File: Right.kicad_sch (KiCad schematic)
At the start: 0 parts

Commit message: finish left side. do a bunch of right side. do right db. change db flat ribbon on both
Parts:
- added C101, C105: 4.7uF, Capacitor_SMD:C_0402_1005Metric, symbol Device:C_Small
- added C102, C103, C107, C108, C109, C110, C111, C112, C113, C114, C115, C116, C118, C120: 1uF, Capacitor_SMD:C_0402_1005Metric, symbol Device:C_Small
- added C104, C106: .1uF, Capacitor_SMD:C_0402_1005Metric, symbol Device:C_Small
- added C117, C119: 2.2uF, Capacitor_SMD:C_0402_1005Metric, symbol Device:C_Small
- added CH_SW101: GESC, marbastlib-choc:SW_choc_HS_1u, symbol MX_Alps_Hybrid:MX-NoLED
- added CH_SW102: 1, marbastlib-choc:SW_choc_HS_1u, symbol MX_Alps_Hybrid:MX-NoLED
- added CH_SW103: 2, marbastlib-choc:SW_choc_HS_1u, symbol MX_Alps_Hybrid:MX-NoLED
- added CH_SW104: 3, marbastlib-choc:SW_choc_HS_1u, symbol MX_Alps_Hybrid:MX-NoLED
- added CH_SW105: 4, marbastlib-choc:SW_choc_HS_1u, symbol MX_Alps_Hybrid:MX-NoLED
- added CH_SW106: 5, marbastlib-choc:SW_choc_HS_1u, symbol MX_Alps_Hybrid:MX-NoLED
- added CH_SW107: TAB, marbastlib-choc:SW_choc_HS_1u, symbol MX_Alps_Hybrid:MX-NoLED
- added CH_SW108: Q, marbastlib-choc:SW_choc_HS_1u, symbol MX_Alps_Hybrid:MX-NoLED
- added CH_SW109: w, marbastlib-choc:SW_choc_HS_1u, symbol MX_Alps_Hybrid:MX-NoLED
- added CH_SW110: E, marbastlib-choc:SW_choc_HS_1u, symbol MX_Alps_Hybrid:MX-NoLED
- added CH_SW111: R, marbastlib-choc:SW_choc_HS_1u, symbol MX_Alps_Hybrid:MX-NoLED
- added CH_SW112: T, marbastlib-choc:SW_choc_HS_1u, symbol MX_Alps_Hybrid:MX-NoLED
- added CH_SW113: CAPS, marbastlib-choc:SW_choc_HS_1u, symbol MX_Alps_Hybrid:MX-NoLED
- added CH_SW114: A, marbastlib-choc:SW_choc_HS_1u, symbol MX_Alps_Hybrid:MX-NoLED
- added CH_SW115: S, marbastlib-choc:SW_choc_HS_1u, symbol MX_Alps_Hybrid:MX-NoLED
- added CH_SW116: D, marbastlib-choc:SW_choc_HS_1u, symbol MX_Alps_Hybrid:MX-NoLED
- added CH_SW117: F, marbastlib-choc:SW_choc_HS_1u, symbol MX_Alps_Hybrid:MX-NoLED
- added CH_SW118: G, marbastlib-choc:SW_choc_HS_1u, symbol MX_Alps_Hybrid:MX-NoLED
- added CH_SW119: SHIFT, marbastlib-choc:SW_choc_HS_1u, symbol MX_Alps_Hybrid:MX-NoLED
- added CH_SW120: Z, marbastlib-choc:SW_choc_HS_1u, symbol MX_Alps_Hybrid:MX-NoLED
- added CH_SW121: X, marbastlib-choc:SW_choc_HS_1u, symbol MX_Alps_Hybrid:MX-NoLED
- added CH_SW122: C, marbastlib-choc:SW_choc_HS_1u, symbol MX_Alps_Hybrid:MX-NoLED
- added CH_SW123: V, marbastlib-choc:SW_choc_HS_1u, symbol MX_Alps_Hybrid:MX-NoLED
- added CH_SW124: B, marbastlib-choc:SW_choc_HS_1u, symbol MX_Alps_Hybrid:MX-NoLED
- added CH_SW125: THUMB 2, marbastlib-choc:SW_choc_HS_1.5u, symbol MX_Alps_Hybrid:MX-NoLED
- added CH_SW126: CTRL, marbastlib-choc:SW_choc_HS_1u, symbol MX_Alps_Hybrid:MX-NoLED
- added CH_SW127: WIN, marbastlib-choc:SW_choc_HS_1u, symbol MX_Alps_Hybrid:MX-NoLED
- added CH_SW128: ALT, marbastlib-choc:SW_choc_HS_1u, symbol MX_Alps_Hybrid:MX-NoLED
- added CH_SW129: FN, marbastlib-choc:SW_choc_HS_1u, symbol MX_Alps_Hybrid:MX-NoLED
- added CH_SW130: THUMB 1, marbastlib-choc:SW_choc_HS_1.25u, symbol MX_Alps_Hybrid:MX-NoLED
- added D101: BAV70_Small, Package_TO_SOT_SMD:SOT-23, symbol marbastlib-various:BAV70_Small
- added D102, D103, D104, D105, D106, D107, D108, D109, D110, D111, D112, D113, D114, D115, D116: ~, Package_TO_SOT_SMD:SOT-23, symbol marbastlib-various:BAV70_Small
- added D117: D, Diode_SMD:D_SOD-123, symbol Device:D_Schottky_Small
- added F101: Polyfuse, Resistor_SMD:R_0805_2012Metric, symbol Device:Polyfuse
- added H101: M.2 Mount (M3), MountingHole:MountingHole_3.2mm_M3_DIN965_Pad, symbol Mechanical:MountingHole_Pad
- added J101: HRO-TYPEC-M12, marbastlib-various:USB_C_Receptacle_HRO_TYPE-C-31-M-14, symbol Connector:USB_C_Receptacle_USB2.0
- added J102, J106: DB FFC, Connector-pat-various:100519220810EHLF, symbol Connector_Generic:Conn_01x08
- added J103: DEBUG, Connector_PinSocket_2.54mm:PinSocket_2x03_P2.54mm_Vertical, symbol Connector_Generic:Conn_02x03_Odd_Even
- added J104: BATTERY, Connector_JST:JST_PH_S2B-PH-SM4-TB_1x02-1MP_P2.00mm_Horizontal, symbol Connector_Generic:Conn_01x02
- added J105: OLED, SSD1306:128x64OLED, symbol Connector_Generic:Conn_01x04
- added J107: SPLIT, Connector-pat-various:Magnetic Pogo 4 pin, symbol Connector_Generic:Conn_01x04
- added J108: EPAPER RIBBON, Connector-pat-various:100519223010ELF, symbol Connector_Generic:Conn_01x30
- added LO101: TapTap Logo, LogoSmall:tt_4mm, symbol Mechanical:MountingHole
- added LO102: MUD LOGO, LogoSmall:LogoSmall_Cu, symbol Switch:SW_SPST
- added M101: M.2_Key_E, m2ngff:m2-bracket-key-e, symbol m2ngff:M.2_Key_E
- added M102, M103: MOUNTING, MountingHole:MountingHole_2.2mm_M2_Pad, symbol Mechanical:MountingHole_Pad
- added MO101, MO102, MO103, MO104, MO105, MO106, MO107: Mousebite, marbastlib-various:mousebites_2mm, symbol Mechanical:MountingHole
- added MX_SW101: GESC, marbastlib-mx:SW_MX_HS_1u, symbol MX_Alps_Hybrid:MX-NoLED
- added MX_SW102: 1, marbastlib-mx:SW_MX_HS_1u, symbol MX_Alps_Hybrid:MX-NoLED
- added MX_SW103: 2, marbastlib-mx:SW_MX_HS_1u, symbol MX_Alps_Hybrid:MX-NoLED
- added MX_SW104: 3, marbastlib-mx:SW_MX_HS_1u, symbol MX_Alps_Hybrid:MX-NoLED
- added MX_SW105: 4, marbastlib-mx:SW_MX_HS_1u, symbol MX_Alps_Hybrid:MX-NoLED
- added MX_SW106: 5, marbastlib-mx:SW_MX_HS_1u, symbol MX_Alps_Hybrid:MX-NoLED
- added MX_SW107: TAB, marbastlib-mx:SW_MX_HS_1u, symbol MX_Alps_Hybrid:MX-NoLED
- added MX_SW108: Q, marbastlib-mx:SW_MX_HS_1u, symbol MX_Alps_Hybrid:MX-NoLED
- added MX_SW109: w, marbastlib-mx:SW_MX_HS_1u, symbol MX_Alps_Hybrid:MX-NoLED
- added MX_SW110: E, marbastlib-mx:SW_MX_HS_1u, symbol MX_Alps_Hybrid:MX-NoLED
- added MX_SW111: R, marbastlib-mx:SW_MX_HS_1u, symbol MX_Alps_Hybrid:MX-NoLED
- added MX_SW112: T, marbastlib-mx:SW_MX_HS_1u, symbol MX_Alps_Hybrid:MX-NoLED
- added MX_SW113: CAPS, marbastlib-mx:SW_MX_HS_1u, symbol MX_Alps_Hybrid:MX-NoLED
- added MX_SW114: A, marbastlib-mx:SW_MX_HS_1u, symbol MX_Alps_Hybrid:MX-NoLED
- added MX_SW115: S, marbastlib-mx:SW_MX_HS_1u, symbol MX_Alps_Hybrid:MX-NoLED
- added MX_SW116: D, marbastlib-mx:SW_MX_HS_1u, symbol MX_Alps_Hybrid:MX-NoLED
- added MX_SW117: F, marbastlib-mx:SW_MX_HS_1u, symbol MX_Alps_Hybrid:MX-NoLED
- added MX_SW118: G, marbastlib-mx:SW_MX_HS_1u, symbol MX_Alps_Hybrid:MX-NoLED
- added MX_SW119: SHIFT, marbastlib-mx:SW_MX_HS_1u, symbol MX_Alps_Hybrid:MX-NoLED
- added MX_SW120: Z, marbastlib-mx:SW_MX_HS_1u, symbol MX_Alps_Hybrid:MX-NoLED
- added MX_SW121: X, marbastlib-mx:SW_MX_HS_1u, symbol MX_Alps_Hybrid:MX-NoLED
- added MX_SW122: C, marbastlib-mx:SW_MX_HS_1u, symbol MX_Alps_Hybrid:MX-NoLED
- added MX_SW123: V, marbastlib-mx:SW_MX_HS_1u, symbol MX_Alps_Hybrid:MX-NoLED
- added MX_SW124: B, marbastlib-mx:SW_MX_HS_1u, symbol MX_Alps_Hybrid:MX-NoLED
- added MX_SW125: THUMB 2, marbastlib-mx:SW_MX_HS_1.5u, symbol MX_Alps_Hybrid:MX-NoLED
- added MX_SW126: CTRL, marbastlib-mx:SW_MX_HS_1u, symbol MX_Alps_Hybrid:MX-NoLED
- added MX_SW127: WIN, marbastlib-mx:SW_MX_HS_1u, symbol MX_Alps_Hybrid:MX-NoLED
- added MX_SW128: ALT, marbastlib-mx:SW_MX_HS_1u, symbol MX_Alps_Hybrid:MX-NoLED
- added MX_SW129: FN, marbastlib-mx:SW_MX_HS_1u, symbol MX_Alps_Hybrid:MX-NoLED
- added MX_SW130: THUMB 1, marbastlib-mx:SW_MX_HS_1.25u, symbol MX_Alps_Hybrid:MX-NoLED
- added MX_SW131: ISO, marbastlib-mx:SW_MX_HS_1u, symbol MX_Alps_Hybrid:MX-NoLED
- added R101, R102: 5.1k, Resistor_SMD:R_0402_1005Metric, symbol Device:R
- added R103, R104: 10K, Resistor_SMD:R_0402_1005Metric, symbol Device:R
- added R105, R106, R107: JUMPER, Resistor_SMD:R_0805_2012Metric, symbol Device:R_Small
- added S101: ISO STAB, Connector-pat-various:STAB_MX_ISONT, symbol marbastlib-mx:MX_stab
- added SW101: Battery Toggle, marbastlib-various:SW_MSK12C02-HB, symbol Switch:SW_SPST
- added U101: SRV05-4, marbastlib-various:SOT-23-6-routable, symbol Power_Protection:SRV05-4
- added U102: XC6206P332MR, Package_TO_SOT_SMD:SOT-23, symbol Regulator_Linear:XC6206PxxxMR
- added UG101, UG102, UG103, UG104, UG105, UG106, UG107, UG108: WS2812_2020, marbastlib-various:LED_WS2812_2020, symbol marbastlib-various:WS2812_2020
- added W101, W102, W103, W104: WINDOW, MountingHole:MountingHole_2.2mm_M2_Pad, symbol Mechanical:MountingHole_Pad
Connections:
- new net: J101.A5 (CC1), R101.2
- new net: CH_SW115.1 (COL), D108.2 (A2), MX_SW115.1 (COL)
- new net: CH_SW113.1 (COL), D107.2 (A2), MX_SW113.1 (COL)
- new net: UG105.1 (DOUT), UG106.3 (DIN)
- new net: UG104.1 (DOUT), UG105.3 (DIN)
- new net: R107.1, UG101.4 (VDD), UG102.4 (VDD), UG103.4 (VDD), UG104.4 (VDD), UG105.4 (VDD), UG106.4 (VDD), UG107.4 (VDD), UG108.4 (VDD)
- new net: UG107.1 (DOUT), UG108.3 (DIN)
- new net: F101.2, J101.A4 (VBUS), J101.A9 (VBUS), J101.B4 (VBUS), J101.B9 (VBUS)
- new net: CH_SW111.1 (COL), D106.2 (A2), MX_SW111.1 (COL)
- new net: J104.1 (Pin_1), SW101.1 (A)
- new net: C106.2, C107.2, J108.11 (Pin_11)
- new net: C118.2, J108.28 (Pin_28)
- new net: CH_SW122.2 (ROW), D111.1 (A1), MX_SW122.2 (ROW)
- new net: CH_SW121.1 (COL), D111.2 (A2), MX_SW121.1 (COL)
- new net: CH_SW114.2 (ROW), D107.1 (A1), MX_SW114.2 (ROW)
- new net: UG101.3 (DIN), UG102.1 (DOUT)
- new net: UG102.3 (DIN), UG103.1 (DOUT)
- new net: CH_SW104.2 (ROW), D102.1 (A1), MX_SW104.2 (ROW)
- new net: CH_SW103.1 (COL), D102.2 (A2), MX_SW103.1 (COL)
- new net: CH_SW112.2 (ROW), D106.1 (A1), MX_SW112.2 (ROW)
- new net: CH_SW119.1 (COL), D110.2 (A2), MX_SW119.1 (COL)
- new net: CH_SW108.2 (ROW), D104.1 (A1), MX_SW108.2 (ROW)
- new net: CH_SW124.2 (ROW), D112.1 (A1), MX_SW124.2 (ROW)
- new net: CH_SW123.1 (COL), D112.2 (A2), MX_SW123.1 (COL)
- new net: J105.1 (Pin_1), R105.1
- new net: C104.1, C105.1, J108.3 (Pin_3), R106.1
- new net: CH_SW130.2 (ROW), D116.1 (A1), MX_SW130.1 (COL), MX_SW131.1 (COL)
- new net: J101.B5 (CC2), R102.1
- new net: C115.1, J108.23 (Pin_23)
- new net: C115.2, J108.22 (Pin_22)
- new net: C112.2, D117.2 (A), J108.15 (Pin_15)
- new net: CH_SW125.2 (ROW), D113.1 (A1), MX_SW125.2 (ROW)
- new net: C109.2, J108.13 (Pin_13)
- new net: CH_SW129.2 (ROW), D115.1 (A1), MX_SW129.2 (ROW)
- new net: CH_SW128.1 (COL), D115.2 (A2), MX_SW128.1 (COL)
- new net: C119.2, J108.29 (Pin_29)
- new net: CH_SW107.1 (COL), D104.2 (A2), MX_SW107.1 (COL)
- new net: C113.1, J108.19 (Pin_19)
- new net: C113.2, J108.18 (Pin_18)
- new net: CH_SW110.2 (ROW), D105.1 (A1), MX_SW110.2 (ROW)
- new net: CH_SW109.1 (COL), D105.2 (A2), MX_SW109.1 (COL)
- new net: CH_SW118.2 (ROW), D109.1 (A1), MX_SW118.2 (ROW)
- new net: UG101.1 (DOUT), UG104.3 (DIN)
- new net: CH_SW126.1 (COL), D114.2 (A2), MX_SW126.1 (COL)
- new net: CH_SW127.2 (ROW), D114.1 (A1), MX_SW127.2 (ROW)
- new net: C108.2, J108.12 (Pin_12)
- new net: CH_SW116.2 (ROW), D108.1 (A1), MX_SW116.2 (ROW)
- new net: UG106.1 (DOUT), UG107.3 (DIN)
- new net: C116.1, J108.25 (Pin_25)
- new net: C116.2, J108.24 (Pin_24)
- new net: CH_SW117.1 (COL), D109.2 (A2), MX_SW117.1 (COL)
- new net: C111.1, J108.17 (Pin_17)
- new net: C111.2, J108.16 (Pin_16)
- new net: CH_SW102.2 (ROW), D101.1 (A1), MX_SW102.2 (ROW)
- new net: CH_SW106.2 (ROW), D103.1 (A1), MX_SW106.2 (ROW)
- new net: CH_SW105.1 (COL), D103.2 (A2), MX_SW105.1 (COL)
- new net: C117.1, J108.27 (Pin_27)
- new net: C117.2, J108.26 (Pin_26)
- new net: C114.1, J108.21 (Pin_21)
- new net: C114.2, J108.20 (Pin_20)
- new net: C110.2, J108.14 (Pin_14)
- new net: C120.2, J108.30 (Pin_30)
- new net: CH_SW101.1 (COL), D101.2 (A2), MX_SW101.1 (COL)
- new net: CH_SW120.2 (ROW), D110.1 (A1), MX_SW120.2 (ROW)
- new net 3.3v: C103.1, R103.2, R104.2, R105.2, R106.2, R107.2, U102.2 (VO)
- new net BATT+: J106.7 (Pin_7), SW101.2 (B)
- new net BUSY: J108.9 (Pin_9), M101.33 (P14)
- new net CLK: J108.5 (Pin_5), M101.46 (P7)
- new net CS: J108.6 (Pin_6), M101.52 (P10)
- new net D+: J101.A6 (D+), J101.B6 (D+), J106.1 (Pin_1), U101.4 (IO3)
- new net D-: J101.A7 (D-), J101.B7 (D-), J106.2 (Pin_2), U101.3 (IO2)
- new net DB_VCC: F101.1, J106.6 (Pin_6), J107.1 (Pin_1), U101.5 (VP)
- new net DC: J108.7 (Pin_7), M101.54 (P11)
- new net DEBUG1: J103.2 (Pin_2), M101.17 (DEBUG1), M101.18 (DEBUG1)
- new net DEBUG2: J103.4 (Pin_4), M101.19 (DEBUG2), M101.20 (DEBUG2)
- new net DEBUG3: J103.6 (Pin_6), M101.21 (DEBUG3), M101.22 (DEBUG3)
- new net DI+: J102.1 (Pin_1), M101.13 (D+), M101.14 (D+)
- new net DI-: J102.2 (Pin_2), M101.15 (D-), M101.16 (D-)
- new net DIN: J108.4 (Pin_4), M101.50 (P9)
- new net GND: C101.2, C102.2, C103.2, C104.2, C105.2, C106.1, C107.1, C108.1, C109.1, C110.1, C112.1, C118.1, C119.1, C120.1, D117.1 (K), H101.1, J101.A1 (GND), J101.A12 (GND), J101.B1 (GND), J101.B12 (GND), J101.S1 (SHIELD), J102.3 (Pin_3), J102.8 (Pin_8), J103.3 (Pin_3), J103.5 (Pin_5), J104.2 (Pin_2), J105.2 (Pin_2), J106.3 (Pin_3), J106.8 (Pin_8), J107.4 (Pin_4), J108.10 (Pin_10), J108.2 (Pin_2), M101.7 (GND), M101.8 (GND), M102.1, M103.1, R101.1, R102.2, U101.2 (VN), U102.1 (GND), UG101.2 (VSS), UG102.2 (VSS), UG103.2 (VSS), UG104.2 (VSS), UG105.2 (VSS), UG106.2 (VSS), UG107.2 (VSS), UG108.2 (VSS), W101.1, W102.1, W103.1, W104.1
- new net I2C1_SCL: J102.5 (Pin_5), J105.4 (Pin_4), M101.58 (P13), R104.1
- new net I2C1_SDA: J102.4 (Pin_4), J105.3 (Pin_3), M101.56 (P12), R103.1
- new net P20: M101.45 (P20)
- new net P21: M101.47 (P21)
- new net P22: M101.49 (P22)
- new net P23: M101.51 (P23)
- new net P24: M101.53 (P24)
- new net P25: M101.55 (P25)
- new net P26: M101.57 (P26)
- new net P27: M101.59 (P27)
- new net RST: J108.8 (Pin_8), M101.35 (P15)
- new net SPLIT_SCL: J106.5 (Pin_5), J107.2 (Pin_2)
- new net SPLIT_SDA: J106.4 (Pin_4), J107.3 (Pin_3)
- new net col0: CH_SW101.2 (ROW), CH_SW107.2 (ROW), CH_SW113.2 (ROW), CH_SW119.2 (ROW), M101.41 (P18), MX_SW101.2 (ROW), MX_SW107.2 (ROW), MX_SW113.2 (ROW), MX_SW119.2 (ROW)
- new net col1: CH_SW102.1 (COL), CH_SW108.1 (COL), CH_SW114.1 (COL), CH_SW120.1 (COL), M101.39 (P17), MX_SW102.1 (COL), MX_SW108.1 (COL), MX_SW114.1 (COL), MX_SW120.1 (COL)
- new net col2: CH_SW103.2 (ROW), CH_SW109.2 (ROW), CH_SW115.2 (ROW), CH_SW121.2 (ROW), CH_SW126.2 (ROW), M101.37 (P16), MX_SW103.2 (ROW), MX_SW109.2 (ROW), MX_SW115.2 (ROW), MX_SW121.2 (ROW), MX_SW126.2 (ROW)
- new net col3: CH_SW104.1 (COL), CH_SW110.1 (COL), CH_SW116.1 (COL), CH_SW122.1 (COL), CH_SW127.1 (COL), M101.48 (P8), MX_SW104.1 (COL), MX_SW110.1 (COL), MX_SW116.1 (COL), MX_SW122.1 (COL), MX_SW127.1 (COL)
- new net col4: CH_SW105.2 (ROW), CH_SW111.2 (ROW), CH_SW117.2 (ROW), CH_SW123.2 (ROW), CH_SW128.2 (ROW), M101.42 (P5), MX_SW105.2 (ROW), MX_SW111.2 (ROW), MX_SW117.2 (ROW), MX_SW123.2 (ROW), MX_SW128.2 (ROW)
- new net col5: CH_SW106.1 (COL), CH_SW112.1 (COL), CH_SW118.1 (COL), CH_SW124.1 (COL), CH_SW129.1 (COL), M101.44 (P6), MX_SW106.1 (COL), MX_SW112.1 (COL), MX_SW118.1 (COL), MX_SW124.1 (COL), MX_SW129.1 (COL)
- new net col6: CH_SW125.1 (COL), CH_SW130.1 (COL), MX_SW125.1 (COL), MX_SW130.2 (ROW), MX_SW131.2 (ROW)
- new net p19: M101.43 (P19)
- new net reset1: LO102.1 (A), M101.1 (RESET1), M101.2 (RESET1)
- new net reset2: LO102.2 (B), M101.3 (RESET2), M101.4 (RESET2)
- new net rgbin: UG103.3 (DIN)
- new net row0: D101.3 (K), D102.3 (K), D103.3 (K), M101.40 (P4)
- new net row1: D104.3 (K), D105.3 (K), D106.3 (K), M101.38 (P3)
- new net row2: D107.3 (K), D108.3 (K), D109.3 (K), M101.36 (P2)
- new net row3: D110.3 (K), D111.3 (K), D112.3 (K), D113.3 (K), M101.34 (P1)
- new net row4: D114.3 (K), D115.3 (K), D116.3 (K), M101.32 (P0)
- new net vbat: J102.7 (Pin_7), M101.23 (VBAT)
- new net vbus: J102.6 (Pin_6), J103.1 (Pin_1), M101.5 (VIN), M101.6 (VIN)
- new net vout: C101.1, C102.1, M101.10 (VOUT), M101.9 (VOUT), U102.3 (VI)
- no-connect marks 0 -> 6
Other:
- note added: "& other tings e.g graphic"
- note added: "BATT"
- note added: "DB"
- note added: "DEBUG"
- note added: "EPAPER"
- note added: "ESD"
- note added: "I2C"
- note added: "I2C F411"
- note added: "I2C1 SCL | SDA B8 | B9 P12 | P13"
- note added: "KEEB"
- note added: "LDO"
- note added: "Logo"
- note added: "Logos"
- note added: "M.2"
- note added: "M.2 Overall"
- note added: "MATRIX"
- note added: "MOUNT"
- note added: "MOUSEBITES"
- note added: "OLED"
- note added: "STAB"
- note added: "Schematic Yoinked from Nicell/epaper-102 Many thanks for making it"
- note added: "UNDERGLOW"
- note added: "USB C"
- note added: "for Mainboard power"
- note added: "for debugging (mainly nrf)"
- note added: "to module"
- company: (none) -> TapTap
- title: (none) -> ISS: International Standard Split

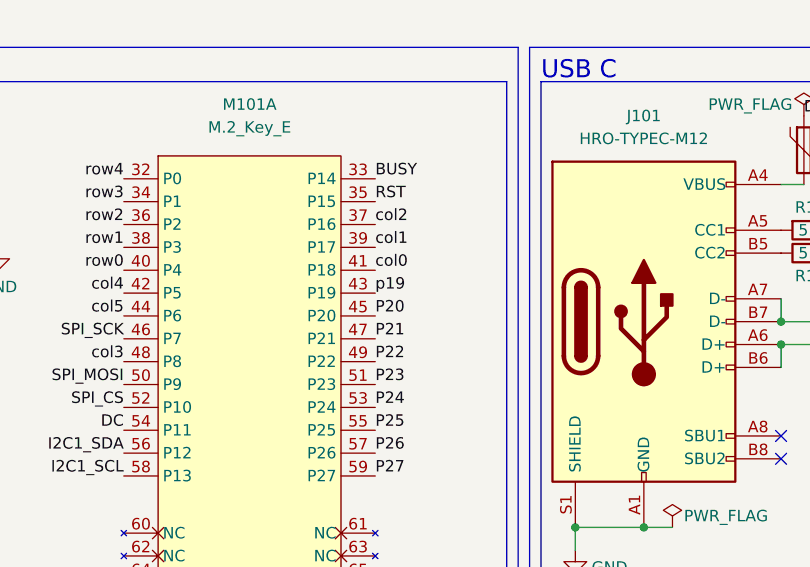
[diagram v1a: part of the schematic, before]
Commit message: finish right. fix some things on left. add teardrops
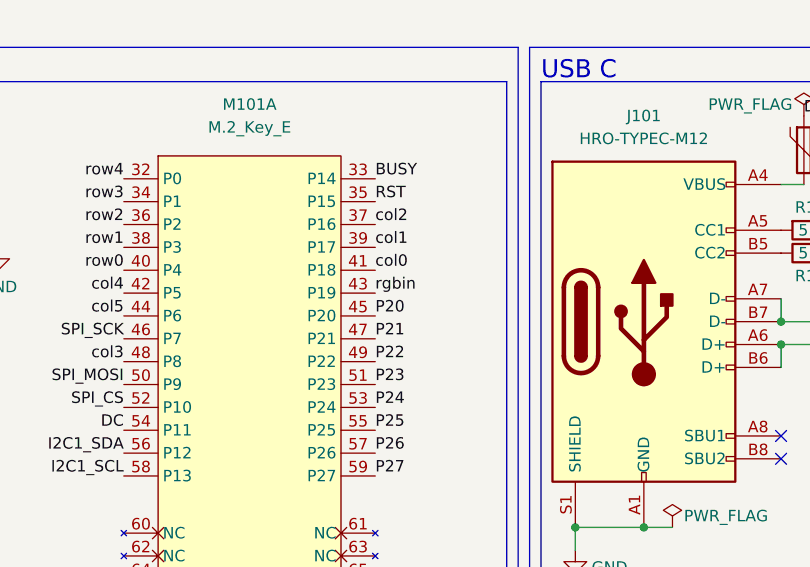
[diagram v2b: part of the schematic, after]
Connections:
- net p19 is gone; now on net rgbin: M101.43 (P19)
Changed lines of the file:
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@@
+    (effects (font (size 1.27 1.27)) (justify left bottom))
+  )
+  (label "rgbin" (at 216.535 46.355 0)
     (effects (font (size 1.27 1.27)) (justify left bottom))
   )
@@
     (effects (font (size 1.27 1.27)) (justify right bottom))
   )
-  (label "p19" (at 216.535 46.355 0)
-    (effects (font (size 1.27 1.27)) (justify left bottom))
-  )
   (label "col1" (at 216.535 41.275 0)

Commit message: add nicer logos and shit
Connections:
- net DB_VCC: now also J107.4 (Pin_4); no longer J107.1 (Pin_1)
- net GND: now also J107.1 (Pin_1); no longer J107.4 (Pin_4)
- net SPLIT_SCL: now also J107.3 (Pin_3); no longer J107.2 (Pin_2)
- net SPLIT_SDA: now also J107.2 (Pin_2); no longer J107.3 (Pin_3)
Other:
- moved on the sheet: J107
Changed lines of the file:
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@@
     (pin "2")
   )
-  (symbol (lib_id "Connector_Generic:Conn_01x04") (at 289.56 125.73 0) (mirror y) (unit 1)
+  (symbol (lib_id "Connector_Generic:Conn_01x04") (at 289.56 128.27 180) (unit 1)
     (in_bom yes) (on_board yes) (fields_autoplaced)
     (property "Reference" "J107" (id 0) (at 289.56 116.84 0))
     (property "Value" "SPLIT" (id 1) (at 289.56 119.38 0))
-    (property "Footprint" "Connector-pat-various:Magnetic Pogo 4 pin" (id 2) (at 289.56 125.73 0)
+    (property "Footprint" "Connector-pat-various:Magnetic Pogo 4 pin" (id 2) (at 289.56 128.27 0)
       (effects (font (size 1.27 1.27)) hide)
     )
-    (property "Datasheet" "~" (id 3) (at 289.56 125.73 0)
+    (property "Datasheet" "~" (id 3) (at 289.56 128.27 0)
       (effects (font (size 1.27 1.27)) hide)
     )
